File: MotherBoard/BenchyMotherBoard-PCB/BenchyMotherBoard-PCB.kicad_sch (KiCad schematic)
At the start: 0 parts

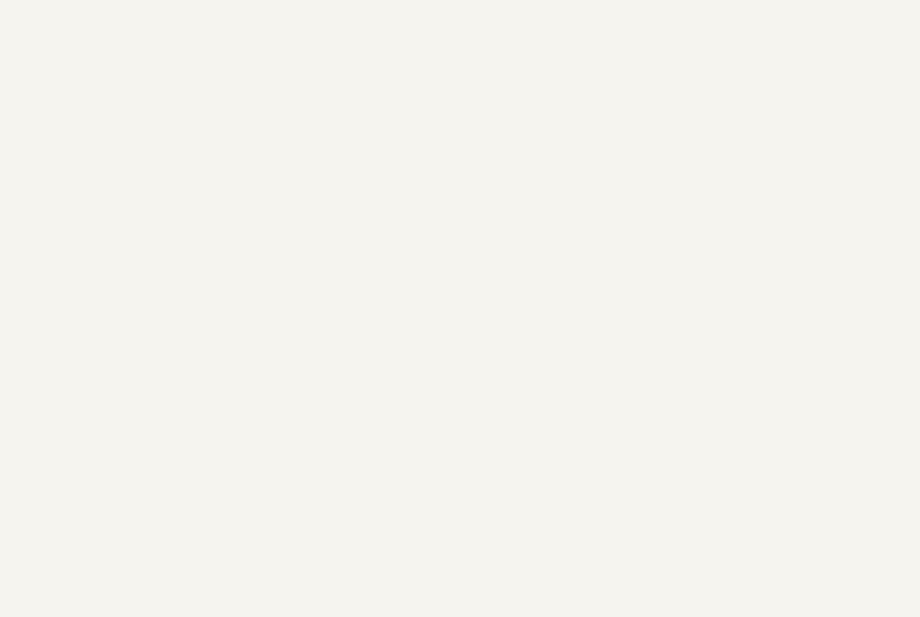
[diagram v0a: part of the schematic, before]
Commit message: (!!WIP!!) Started schematic and block diagram
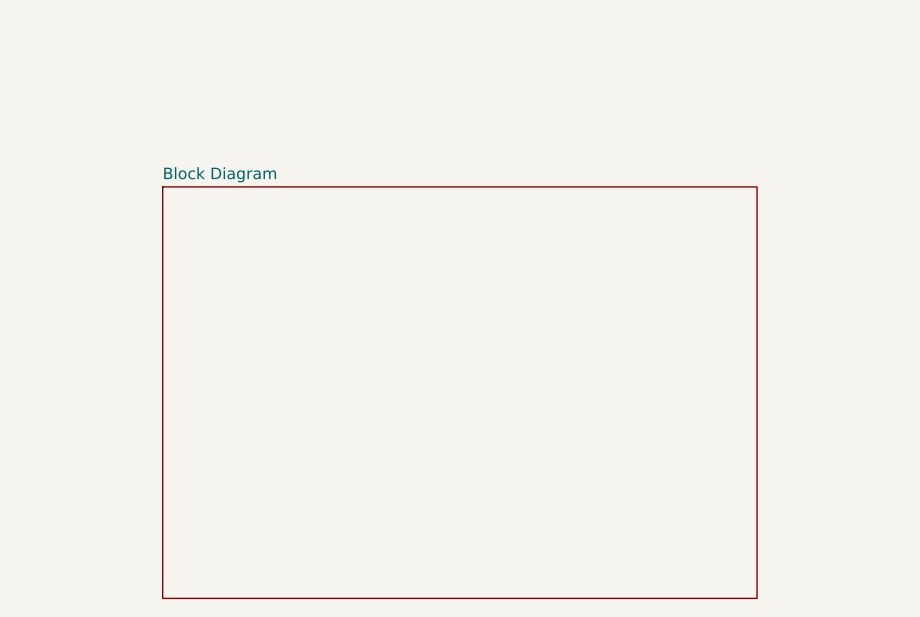
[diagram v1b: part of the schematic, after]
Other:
- added sheet Block Diagram (BlockDiagram.kicad_sch)
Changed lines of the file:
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@@
+    )
+  )
+  (sheet (at 57.15 129.54) (size 66.04 45.72) (fields_autoplaced)
+    (stroke (width 0.1524) (type solid))
+    (fill (color 0 0 0 0.0000))
+    (property "Sheetname" "Block Diagram" (at 57.15 128.8284 0)
+      (effects (font (size 1.27 1.27)) (justify left bottom))
+    )
+    (property "Sheetfile" "BlockDiagram.kicad_sch" (at 57.15 175.8446 0)
+      (effects (font (size 1.27 1.27)) (justify left top) hide)
+    )
+    (instances
+      (project "BenchyMotherBoard-PCB"
+        (path "/2ea077fe-b0e6-467f-a1c1-8336ebdb7a86" (page "7"))
+      )
     )
   )

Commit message: (WIP) Finish more of the PS schematic
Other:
- sheet MEMORY renamed DDR MEMORY
- removed sheet Block Diagram
- added sheet AUDIO (Audio.kicad_sch)
- added sheet DISPLAY (Display.kicad_sch)
- added sheet ETHERNET (Ethernet.kicad_sch)
- added sheet eMMC MEMORY (emmc_memory.kicad_sch)
- note added: "REMOVE ALL THE HEIR. LABELS"
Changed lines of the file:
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@@
 (kicad_sch (version 20230121) (generator eeschema)
-  (paper "User" 310.007 124.993)
+  (paper "A4")
   (title_block
     (title "Benchy Reloaded")
-    (rev "REV2")
+    (rev "REV4")
     (company "Daxxn Industries")
   )
@@
     (effects (font (size 4 4) bold) (justify left bottom) (href "#3"))
   )
+  (text "REMOVE ALL THE HEIR. LABELS" (at 165.1 29.21 0)
+    (effects (font (size 1.016 1.016)) (justify left bottom))
+  )
   (text "INPUT | OUTPUT" (at 115.57 36.83 0)
     (effects (font (size 3 3) bold) (justify left bottom) (href "#4"))
   )
+  (sheet (at 100.33 113.03) (size 39.37 34.29) (fields_autoplaced)
+    (stroke (width 0.1524) (type solid))
+    (fill (color 0 0 0 0.0000))
+    (property "Sheetname" "AUDIO" (at 100.33 112.3184 0)
+      (effects (font (size 1.27 1.27)) (justify left bottom))
+    )
+    (property "Sheetfile" "Audio.kicad_sch" (at 100.33 147.9046 0)
+      (effects (font (size 1.27 1.27)) (justify left top) hide)
+    )
+    (instances
+      (project "BenchyMotherBoard-PCB"
+        (path "/2ea077fe-b0e6-467f-a1c1-8336ebdb7a86" (page "10"))
+      )
+    )
+  )
+  (sheet (at 106.68 154.94) (size 53.34 34.29) (fields_autoplaced)
+    (stroke (width 0.1524) (type solid))
+    (fill (color 0 0 0 0.0000))
+    (property "Sheetname" "ETHERNET" (at 106.68 154.2284 0)
+      (effects (font (size 1.27 1.27)) (justify left bottom))
+    )
+    (property "Sheetfile" "Ethernet.kicad_sch" (at 106.68 189.8146 0)
+      (effects (font (size 1.27 1.27)) (justify left top) hide)
+    )
+    (instances
+      (project "BenchyMotherBoard-PCB"
+        (path "/2ea077fe-b0e6-467f-a1c1-8336ebdb7a86" (page "11"))
+      )
+    )
+  )
+  (sheet (at 250.19 119.38) (size 27.94 25.4) (fields_autoplaced)
+    (stroke (width 0.1524) (type solid))
+    (fill (color 0 0 0 0.0000))
+    (property "Sheetname" "DISPLAY" (at 250.19 118.6684 0)
+      (effects (font (size 1.27 1.27)) (justify left bottom))
+    )
+    (property "Sheetfile" "Display.kicad_sch" (at 250.19 145.3646 0)
+      (effects (font (size 1.27 1.27)) (justify left top) hide)
+    )
+    (instances
+      (project "BenchyMotherBoard-PCB"
+        (path "/2ea077fe-b0e6-467f-a1c1-8336ebdb7a86" (page "9"))
+      )
+    )
+  )
   (sheet (at 13.97 44.45) (size 36.83 50.8)
     (stroke (width 0.1524) (type solid))
     (fill (color 0 0 0 0.0000))
-    (property "Sheetname" "MEMORY" (at 13.97 44.45 0)
+    (property "Sheetname" "DDR MEMORY" (at 13.97 44.45 0)
       (effects (font (size 1 1) bold) (justify left bottom))
     )
@@
       (project "BenchyMotherBoard-PCB"
         (path "/2ea077fe-b0e6-467f-a1c1-8336ebdb7a86" (page "4"))
-      )
-    )
-  )
-  (sheet (at 57.15 129.54) (size 66.04 45.72) (fields_autoplaced)
-    (stroke (width 0.1524) (type solid))
-    (fill (color 0 0 0 0.0000))
-    (property "Sheetname" "Block Diagram" (at 57.15 128.8284 0)
-      (effects (font (size 1.27 1.27)) (justify left bottom))
-    )
-    (property "Sheetfile" "BlockDiagram.kicad_sch" (at 57.15 175.8446 0)
-      (effects (font (size 1.27 1.27)) (justify left top) hide)
-    )
-    (instances
-      (project "BenchyMotherBoard-PCB"
-        (path "/2ea077fe-b0e6-467f-a1c1-8336ebdb7a86" (page "7"))
       )
     )
@@
       )
     )
+  )
+  (sheet (at 182.88 111.76) (size 52.07 36.83) (fields_autoplaced)
+    (stroke (width 0.1524) (type solid))
+    (fill (color 0 0 0 0.0000))
+    (property "Sheetname" "eMMC MEMORY" (at 182.88 111.0484 0)
+      (effects (font (size 1.27 1.27)) (justify left bottom))
+    )
+    (property "Sheetfile" "emmc_memory.kicad_sch" (at 182.88 149.1746 0)
+      (effects (font (size 1.27 1.27)) (justify left top) hide)
+    )
+    (instances
+      (project "BenchyMotherBoard-PCB"
+        (path "/2ea077fe-b0e6-467f-a1c1-8336ebdb7a86" (page "12"))
+      )
+    )

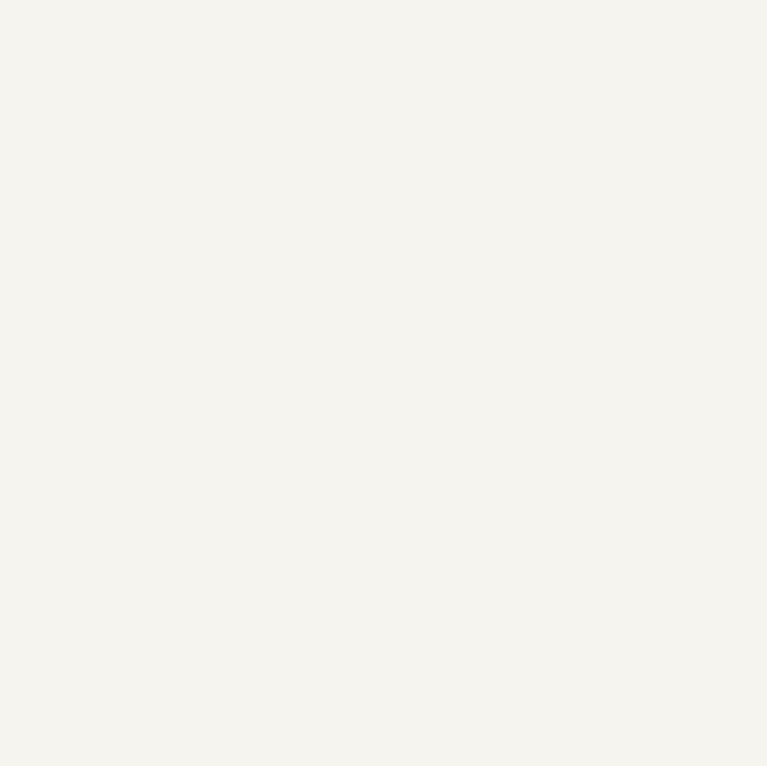
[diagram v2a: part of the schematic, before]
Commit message: (WIP) Complete most of the PS and boot schematics
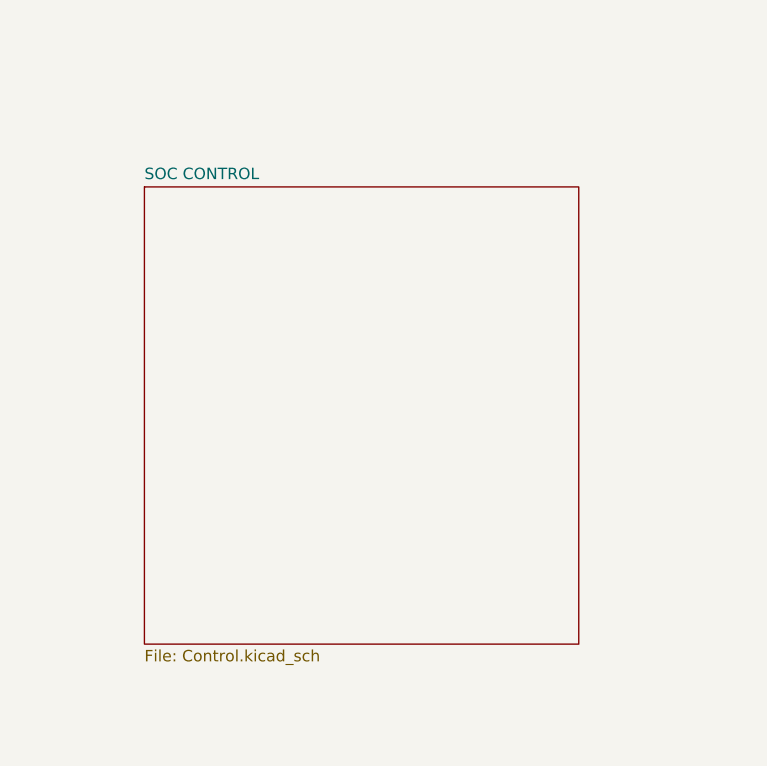
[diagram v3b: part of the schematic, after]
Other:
- added sheet SOC CONTROL (Control.kicad_sch)
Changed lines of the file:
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@@
     (effects (font (size 3 3) bold) (justify left bottom) (href "#4"))
+  )
+  (sheet (at 27.94 127) (size 48.26 50.8) (fields_autoplaced)
+    (stroke (width 0.1524) (type solid))
+    (fill (color 0 0 0 0.0000))
+    (property "Sheetname" "SOC CONTROL" (at 27.94 126.2884 0)
+      (effects (font (size 1.27 1.27)) (justify left bottom))
+    )
+    (property "Sheetfile" "Control.kicad_sch" (at 27.94 178.3846 0)
+      (effects (font (size 1.27 1.27)) (justify left top))
+    )
+    (instances
+      (project "BenchyMotherBoard-PCB"
+        (path "/2ea077fe-b0e6-467f-a1c1-8336ebdb7a86" (page "11"))
+      )
+    )
   )
   (sheet (at 100.33 113.03) (size 39.37 34.29) (fields_autoplaced)

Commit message: (WIP) Almost done with schematic
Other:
- sheet USB | DISPLAY renamed USB
- sheet COMMUNICATIONS ports: added none; removed ELOAD-BUS{SDA SCK}, LOGIC-BUS{SDA SCK}, PWR-BUS{SDA SCK}, RELAY-BUS[1..6], SWITCHER-BUS{SDA SCK}
- sheet INPUT | OUTPUT ports: added none; removed DISP-BUS{BRIGHT RESET TE}, ELOAD-BUS{SDA SCK}, LOGIC-BUS{SDA SCK}, PWR-BUS{SDA SCK}, RELAY-BUS[1..6], SM-BUS{RX TX}, SWITCHER-BUS{SDA SCK}, USB-BUS{RESET SDA SCK}
- sheet POWER ports: added none; removed SM-BUS{RX TX}
- sheet USB ports: added none; removed DISP-BUS{BRIGHT RESET TE}, USB-BUS{RESET SDA SCK}
- note added: "USB"
- note removed: "USB | DISP"
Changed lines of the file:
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@@
     (company "Daxxn Industries")
-  )
-  (bus (pts (xy 177.8 67.31) (xy 190.5 67.31))
-    (stroke (width 0) (type default))
-  )
-  (bus (pts (xy 177.8 41.91) (xy 190.5 41.91))
-    (stroke (width 0) (type default))
-  )
-  (bus (pts (xy 177.8 34.29) (xy 190.5 34.29))
-    (stroke (width 0) (type default))
-  )
-  (bus (pts (xy 101.6 57.15) (xy 114.3 57.15))
-    (stroke (width 0) (type default))
-  )
-  (bus (pts (xy 177.8 44.45) (xy 190.5 44.45))
-    (stroke (width 0) (type default))
-  )
-  (bus (pts (xy 177.8 36.83) (xy 190.5 36.83))
-    (stroke (width 0) (type default))
-  )
-  (bus (pts (xy 177.8 39.37) (xy 190.5 39.37))
-    (stroke (width 0) (type default))
-  )
-  (bus (pts (xy 177.8 69.85) (xy 190.5 69.85))
-    (stroke (width 0) (type default))
   )
   (text_box ""
@@
     (effects (font (size 1.016 1.016) bold) (justify left top) (href "#3"))
   )
-  (text "USB | DISP" (at 240.03 68.58 0)
+  (text "USB" (at 240.03 68.58 0)
     (effects (font (size 3 3) bold) (justify right bottom) (href "#5"))
   )
@@
     (stroke (width 0.1524) (type solid))
     (fill (color 0 0 0 0.0000))
-    (property "Sheetname" "USB | DISPLAY" (at 190.5 63.5 0)
+    (property "Sheetname" "USB" (at 190.5 63.5 0)
       (effects (font (size 1 1) bold) (justify left bottom))
     )
     (property "Sheetfile" "usb.kicad_sch" (at 190.5 114.8846 0)
       (effects (font (size 1.27 1.27)) (justify left top) hide)
-    )
-    (pin "DISP-BUS{BRIGHT RESET TE}" input (at 190.5 67.31 180)
-      (effects (font (size 1.016 1.016)) (justify left))
-    )
-    (pin "USB-BUS{RESET SDA SCK}" input (at 190.5 69.85 180)
-      (effects (font (size 1.016 1.016)) (justify left))
     )
     (instances
@@
     (property "Sheetfile" "gpio.kicad_sch" (at 114.3 108.5346 0)
       (effects (font (size 1.27 1.27)) (justify left top) hide)
-    )
-    (pin "SM-BUS{RX TX}" input (at 114.3 57.15 180)
-      (effects (font (size 1.016 1.016)) (justify left))
-    )
-    (pin "USB-BUS{RESET SDA SCK}" input (at 177.8 69.85 0)
-      (effects (font (size 1.016 1.016)) (justify right))
-    )
-    (pin "LOGIC-BUS{SDA SCK}" input (at 177.8 36.83 0)
-      (effects (font (size 1.016 1.016)) (justify right))
-    )
-    (pin "DISP-BUS{BRIGHT RESET TE}" input (at 177.8 67.31 0)
-      (effects (font (size 1.016 1.016)) (justify right))
-    )
-    (pin "ELOAD-BUS{SDA SCK}" input (at 177.8 39.37 0)
-      (effects (font (size 1.016 1.016)) (justify right))
-    )
-    (pin "RELAY-BUS[1..6]" input (at 177.8 34.29 0)
-      (effects (font (size 1.016 1.016)) (justify right))
-    )
-    (pin "PWR-BUS{SDA SCK}" input (at 177.8 41.91 0)
-      (effects (font (size 1.016 1.016)) (justify right))
-    )
-    (pin "SWITCHER-BUS{SDA SCK}" input (at 177.8 44.45 0)
-      (effects (font (size 1.016 1.016)) (justify right))
     )
     (instances
@@
       (effects (font (size 1.27 1.27)) hide)
     )
-    (pin "SM-BUS{RX TX}" input (at 101.6 57.15 0)
-      (effects (font (size 1.016 1.016)) (justify right))
-    )
     (instances
       (project "BenchyMotherBoard-PCB"
@@
       (effects (font (size 1.27 1.27)) (justify left top) hide)
     )
-    (pin "RELAY-BUS[1..6]" input (at 190.5 34.29 180)
-      (effects (font (size 1.016 1.016)) (justify left))
-    )
-    (pin "LOGIC-BUS{SDA SCK}" input (at 190.5 36.83 180)
-      (effects (font (size 1.016 1.016)) (justify left))
-    )
-    (pin "ELOAD-BUS{SDA SCK}" input (at 190.5 39.37 180)
-      (effects (font (size 1.016 1.016)) (justify left))
-    )
-    (pin "PWR-BUS{SDA SCK}" input (at 190.5 41.91 180)
-      (effects (font (size 1.016 1.016)) (justify left))
-    )
-    (pin "SWITCHER-BUS{SDA SCK}" input (at 190.5 44.45 180)
-      (effects (font (size 1.016 1.016)) (justify left))
-    )
     (instances
